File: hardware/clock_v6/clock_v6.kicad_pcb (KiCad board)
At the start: 2 copper layers, 119 x 92 mm, 153 parts, among them J1 RJ45, J12 Conn_01x06, J2 Conn_01x06_Pin, J4 Conn_01x04_Pin, J5 Conn_01x06_Pin, J6 Conn_01x04_Pin, J7 Conn_01x04_Pin, J8 Conn_01x02, Q10 2N7002, Q9 2N7002, U1 ADA4807-1, U10 STM32F405RGTx, U11 AMS1117-3.3, U12 BA50DD0WHFP-TR, U13 M24C02-RMN, U2 SN74LVC1G14DBV, U3 SN74LVC1G14DBV, U4 ADA4807-1, U5 ADA4807-1, U6 TLV3603DCKR, U7 SN74LVC1G14DBV, U8 TLV3603DCKR, U9 L78L05_SOT89, Y1 AOCJY4A-10.000MHZ-SW, Y2 16MHz

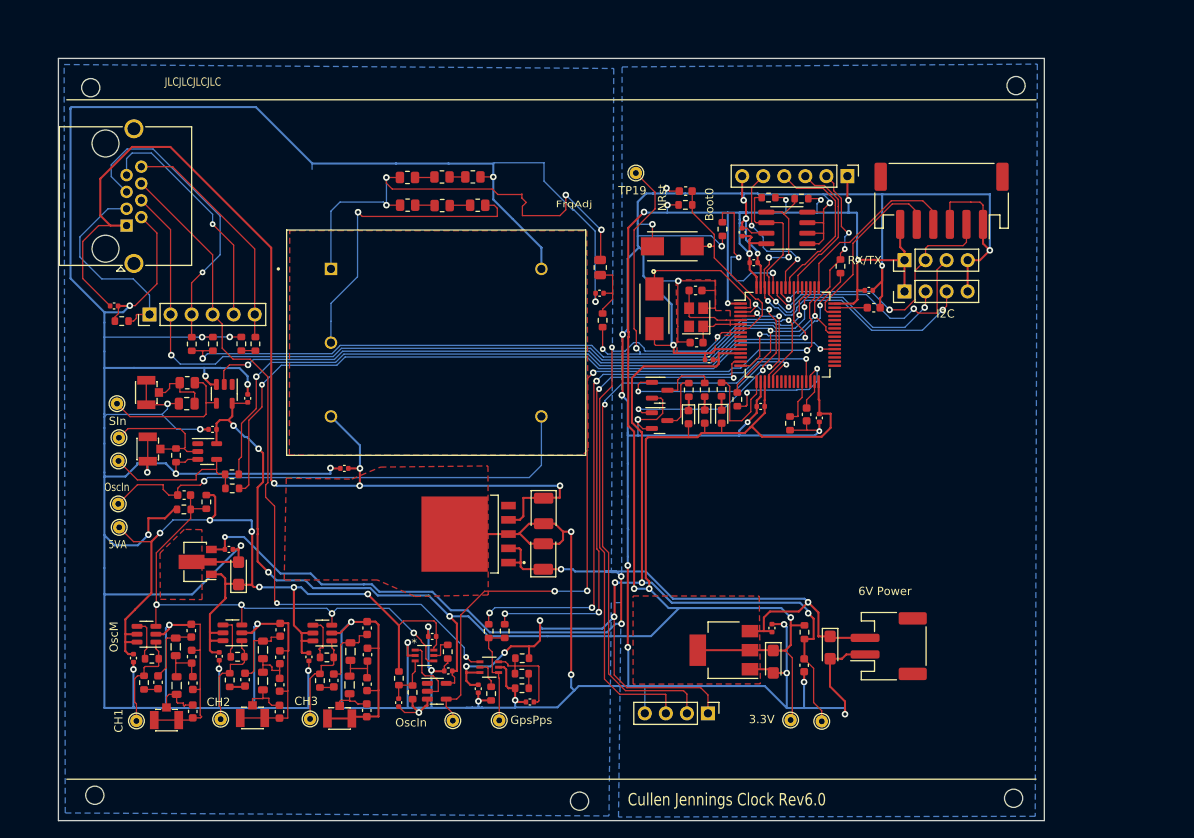
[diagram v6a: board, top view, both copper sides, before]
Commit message: add BNC connectors to clock board
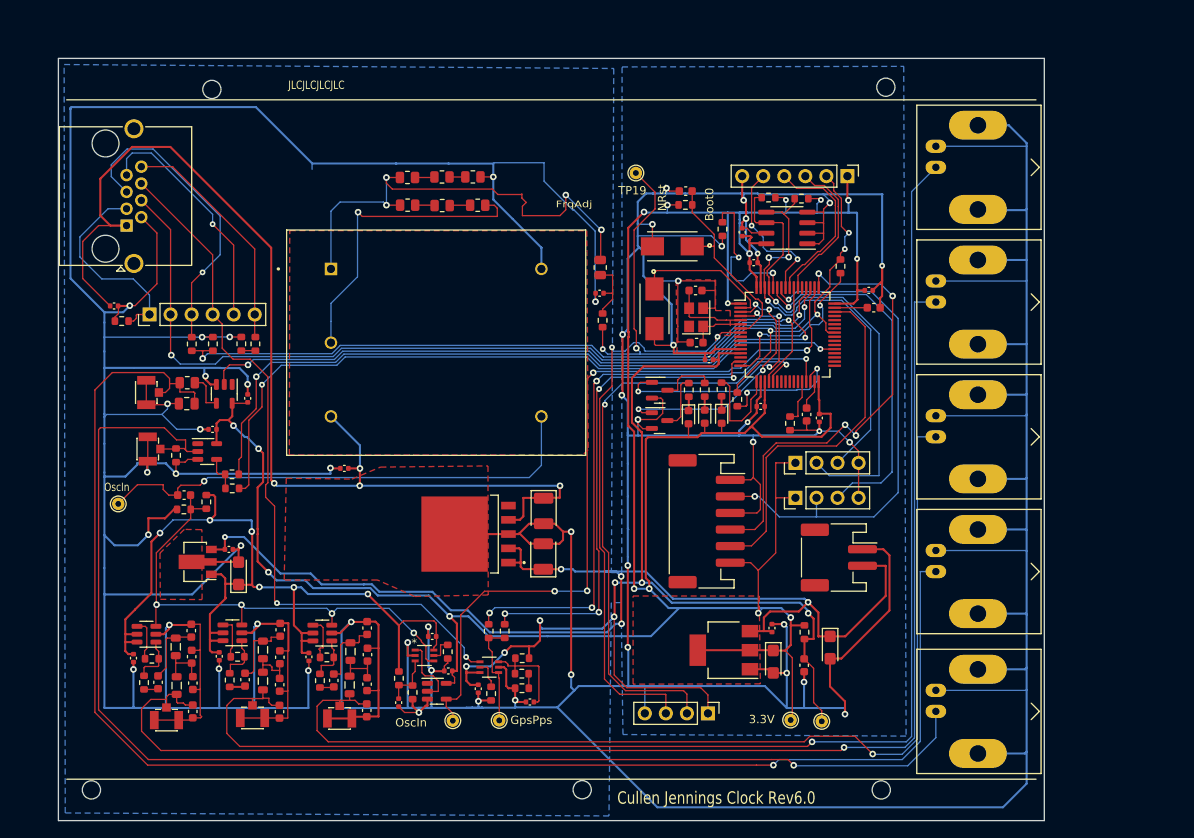
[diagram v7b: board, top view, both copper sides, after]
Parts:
- removed TP15, TP2, TP3, TP4, TP5, TP6, TP7: ~, TestPoint:TestPoint_THTPad_D1.5mm_Drill0.7mm
- added J10: KH-BNC50-3511, blinky_footprints:BNC_Amphenol_B6252HB-NPP3G-50_Horizontal-CJ, F.Cu at (203.4, 99.9)
- added J11: KH-BNC50-3511, blinky_footprints:BNC_Amphenol_B6252HB-NPP3G-50_Horizontal-CJ, F.Cu at (203.4, 51.1)
- added J13: KH-BNC50-3511, blinky_footprints:BNC_Amphenol_B6252HB-NPP3G-50_Horizontal-CJ, F.Cu at (203.4, 67.4)
- added J3: KH-BNC50-3511, blinky_footprints:BNC_Amphenol_B6252HB-NPP3G-50_Horizontal-CJ, F.Cu at (203.4, 83.7)
- added J9: KH-BNC50-3511, blinky_footprints:BNC_Amphenol_B6252HB-NPP3G-50_Horizontal-CJ, F.Cu at (203.4, 116.8)
- moved J12 48.0 mm to (173.2, 93.9), turned to -90 degrees
- moved J6 31.6 mm to (184.0, 91.0)
- moved J7 24.5 mm to (184.0, 86.8)
- moved H4 16.0 mm to (194.3, 126.3)
- moved H2 15.7 mm to (194.9, 41.5)
- moved H1 14.6 mm to (113.5, 41.7)
- moved J8 12.3 mm to (189.2, 98.2), turned to -90 degrees
- moved H3 1.41 mm to (158.2, 126.3)
- moved H5 0.77 mm to (99.0, 126.3)
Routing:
- net GND: track 971.0 -> 1229.8 mm, vias 50 -> 51
- net Net-(J10-In): track 7.61 -> 183.2 mm, vias 0 -> 1
- net Net-(J11-In): track 5.80 -> 166.4 mm, vias 0 -> 1
- net Net-(J13-In): track 5.93 -> 161.9 mm, vias 0 -> 1
- net Net-(J9-In): track 15.2 -> 159.4 mm, vias 0 -> 1
- net Net-(J3-In): track 4.94 -> 124.6 mm, vias 0 -> 1
- net /SWDCLK: track 22.0 -> 56.0 mm, vias 0 -> 4
- net /USB_RX: track 33.1 -> 62.7 mm
- net /SWDIO: track 22.2 -> 43.3 mm
- net /SCL: track 41.8 -> 59.0 mm, vias 2 -> 1
- net +3.3V: track 340.8 -> 355.1 mm, vias 15 -> 16
- net Net-(R63-Pad2): track 18.1 -> 4.41 mm
- net /USB_TX: track 30.2 -> 43.5 mm, vias 2 -> 1
- net Net-(R4-Pad1): track 17.7 -> 4.82 mm
- net +6V: track 126.3 -> 137.1 mm
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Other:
- board text removed: "5VA"
- board text removed: "6V Power"
- board text removed: "CH1"
- board text removed: "CH2"
- board text removed: "CH3"
- board text removed: "I2C"
- board text removed: "OscM"
- board text removed: "RX/TX"
- board text removed: "SIn"

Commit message: clean up clock v6
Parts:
- moved J10 0.46 mm to (203.4, 100.4)
- moved J3 0.31 mm to (203.4, 84.0)
- moved J13 0.15 mm to (203.4, 67.6)
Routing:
- net /SCL: track 59.0 -> 63.0 mm
- net +3.3V: track 355.1 -> 351.5 mm
- net /USB_RX: track 62.7 -> 60.2 mm
- net +6V: track 137.1 -> 134.9 mm
- net Net-(J9-In): track 159.4 -> 161.3 mm
- net /SDA: track 51.4 -> 53.3 mm
- net Net-(J13-In): track 161.9 -> 160.4 mm
- net /GPS_TX1H: track 37.4 -> 36.1 mm
- net /AUD_OUT: track 73.1 -> 74.3 mm
- net /GPS_EN: track 25.2 -> 24.3 mm
- net CLK: track 92.7 -> 93.4 mm
- net Net-(J10-In): track 183.2 -> 183.7 mm, vias 1 -> 0
